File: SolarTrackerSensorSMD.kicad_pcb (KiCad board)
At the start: 2 copper layers, 94 x 70 mm, 81 parts, among them J1 Conn_01x03_Male, J10 Conn_01x01_Male, J11 Conn_01x01_Male, J12 Conn_01x01_Male, J13 Conn_01x01_Male, J14 Conn_01x01_Male, J15 Conn_01x05_Male, J16 Conn_01x05_Male, J17 Conn_01x01_Male, J18 Conn_01x01_Male, J19 Conn_01x01_Male, J2 Conn_01x03_Male, J20 Conn_01x01_Male, J21 Conn_01x01_Male, J22 Conn_01x01_Male, J23 Conn_01x01_Male, J24 Conn_01x01_Male, J3 Conn_01x03_Male, J4 Conn_01x03_Male, J5 Conn_01x07_Male, J6 Conn_01x05_Male, J7 Conn_01x01_Male, J8 Conn_01x01_Male, J9 Conn_01x01_Male, Q1 Q_Photo_NPN, Q2 Q_Photo_NPN, Q3 Q_Photo_NPN, Q4 Q_Photo_NPN, Q5 Q_Photo_NPN, Q6 Q_Photo_NPN, Q7 Q_Photo_NPN, Q8 Q_Photo_NPN, U1 LM339, U2 7404, U3 7408, U4 7408, U5 7432

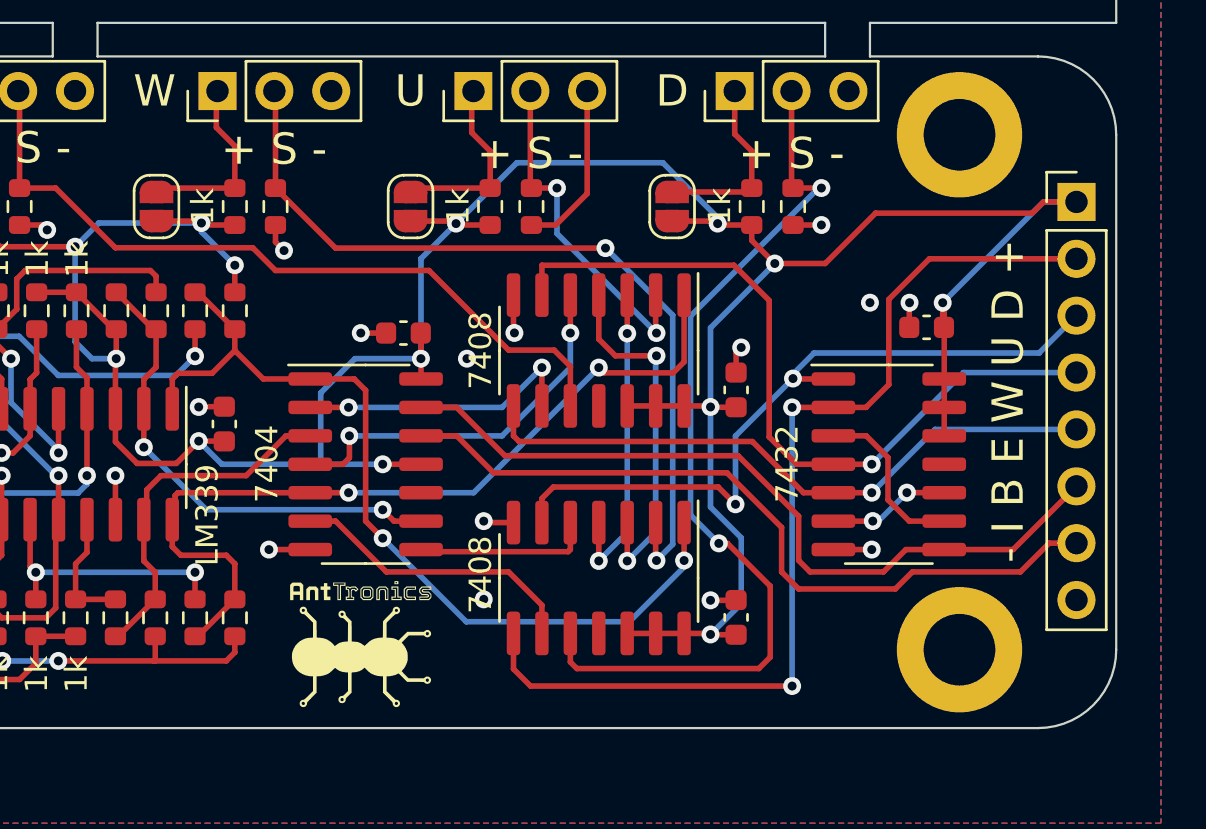
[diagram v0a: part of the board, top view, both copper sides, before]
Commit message: Replace Idle with Busy_UD & Busy_EW
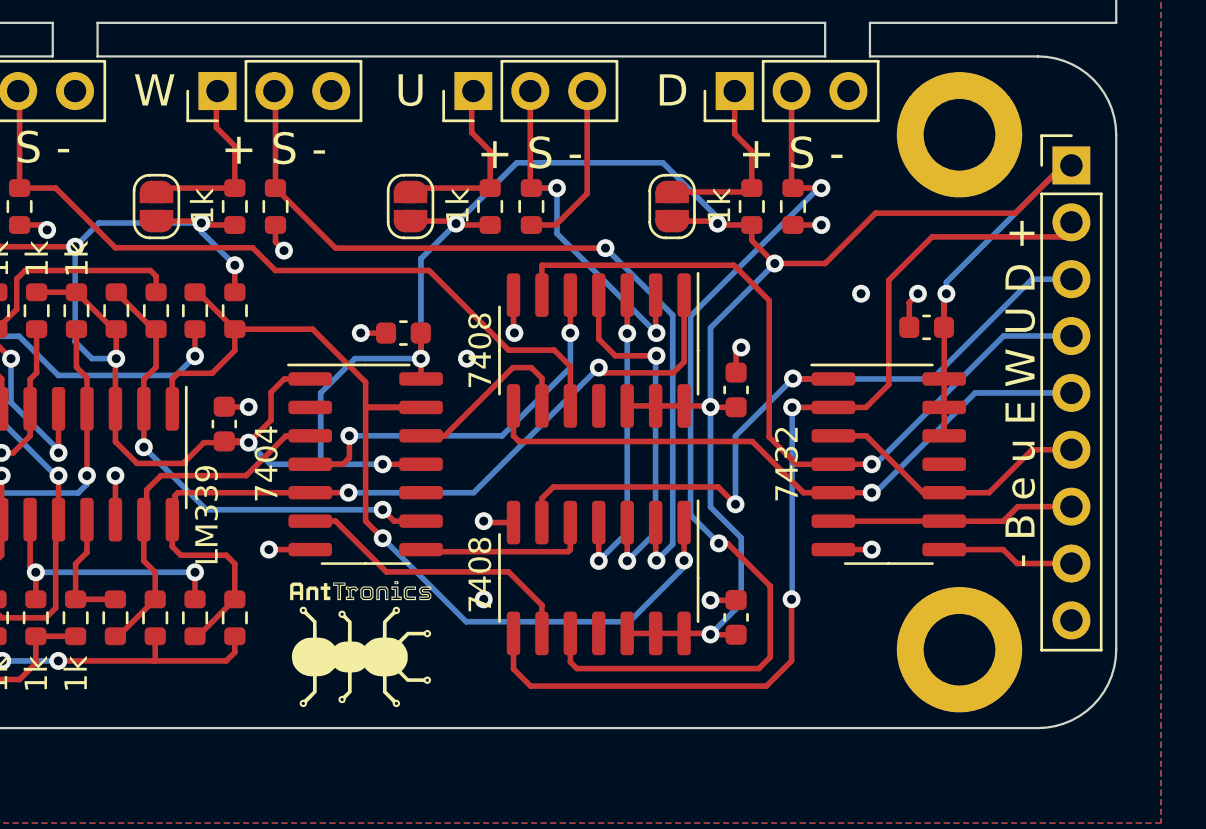
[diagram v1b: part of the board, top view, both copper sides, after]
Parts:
- J5: footprint Connector_PinHeader_2.54mm:PinHeader_1x08_P2.54mm_Vertical -> Connector_PinHeader_2.54mm:PinHeader_1x09_P2.54mm_Vertical
- moved J5 1.65 mm to (151.0, 95.9)
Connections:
- J5 pad 6: /BUSY -> /BUSY_UD
- J5 pad 7: /IDLE -> /BUSY_EW
- J5 pad 8: GND -> /BUSY
- U2 pad 1: /CW -> VCC
- U2 pad 12: /IDLE -> /NCW
- U2 pad 13: /BUSY -> /CW
- U2 pad 2: /NCW -> unconnected-(U2-Pad2)
- U5 pad 10: Net-(U5-Pad10) -> /BUSY_UD
- U5 pad 3: Net-(U5-Pad3) -> /BUSY_UD
- U5 pad 6: Net-(U5-Pad10) -> /BUSY_EW
- U5 pad 9: Net-(U5-Pad3) -> /BUSY_EW
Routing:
- net /IDLE: track 34.1 -> 0.00 mm
- net /BUSY: track 35.1 -> 6.19 mm
- net /BUSY_UD: track 0.00 -> 12.7 mm
- net /BUSY_EW: track 0.00 -> 11.2 mm
- net Net-(U5-Pad3): track 7.63 -> 0.00 mm
- net VCC: track 192.5 -> 199.8 mm
- net /CW: track 39.6 -> 45.1 mm
- net Net-(U5-Pad10): track 5.48 -> 0.00 mm, vias 2 -> 0
- net /NCW: track 12.8 -> 8.10 mm, vias 2 -> 0
- net /OW: track 34.2 -> 34.9 mm
- net /OU: track 32.7 -> 33.3 mm
- net /OD: track 44.5 -> 45.0 mm
- net GND: track 44.8 -> 45.3 mm
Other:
- board text added: "- B e u E W U D +"
- board text removed: "- I B E W U D +"

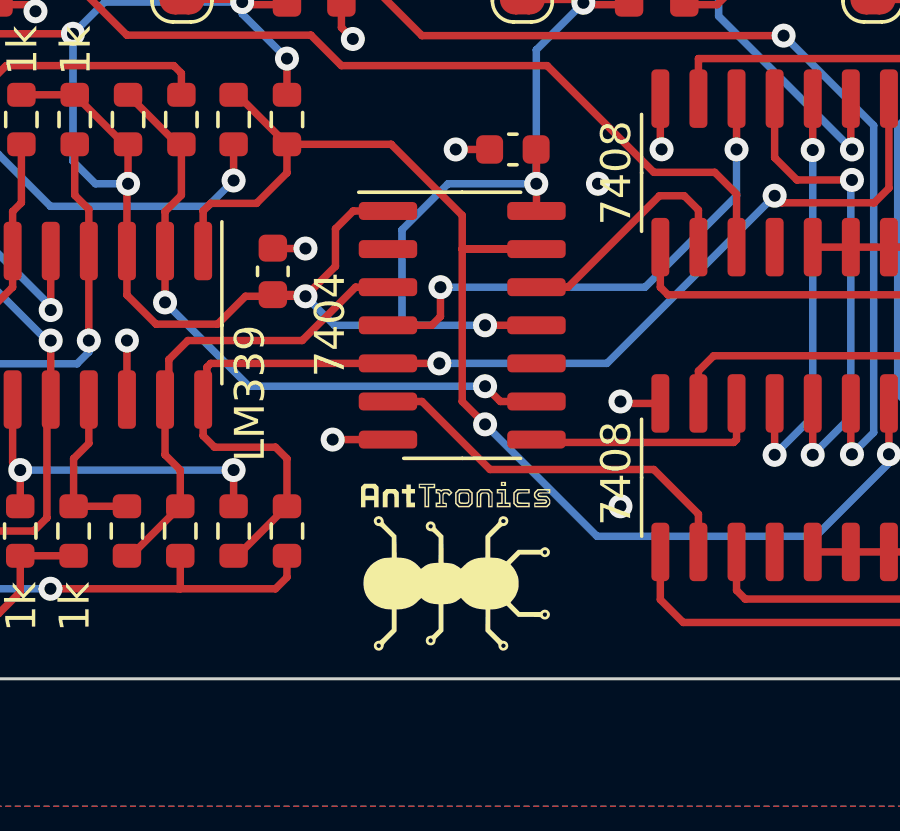
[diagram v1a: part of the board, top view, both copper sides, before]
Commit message: Add licence & reshuffle silkscreen graphics
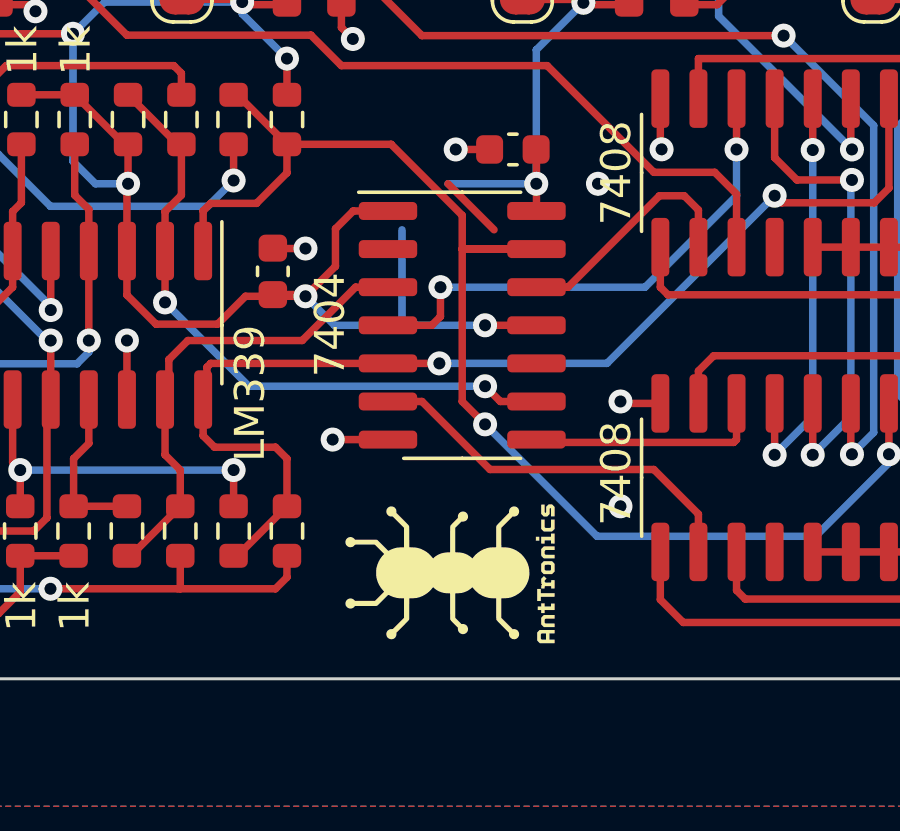
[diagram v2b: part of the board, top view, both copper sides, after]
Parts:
- removed the G*** at (119.2, 117.2)
- removed the G*** at (119.8, 102.0)
- removed the G*** at (106.5, 116.5)
- added G***: LOGO, AntTronics_Graphics:AntTronics_logo_tall_5x7, F.Cu at (119.0, 117.5)
- added G***: LOGO, LOGO, B.Cu at (125.2, 111.0)
- added G***: LOGO, AntTronics_Graphics:AntTronics_logo_square_10x10, B.Cu at (136.2, 104.5)
- added REF**: OSHW-Logo_5.7x6mm_SilkScreen, Symbol:OSHW-Logo_5.7x6mm_SilkScreen, B.Cu at (138.5, 116.0)
- moved G*** 15.7 mm to (116.2, 101.8), turned to 180 degrees
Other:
- board text added: "Copyright © 2023 Antonios Vamporakis <ant@anttronics.com> Licensed under CERN-OHL-S v2 or any later version https://github.com/anttronics/SolarTrackerSensor"
- board text added: "SPDX-FileCopyrightText: 2023 Antonios Vamporakis <ant@anttronics.com> SPDX-License-Identifier: CERN-OHL-S-2.0+ This source is distributed WITHOUT ANY EXPRESS OR IMPLIED WARRANTY, INCLUDING OF MERCHANTABILITY, SATISFACTORY QUALITY AND FITNESS FOR A PARTICULAR PURPOSE. Please see the CERN-OHL-S v2 for applicable conditions. Source location: https://github.com/anttronics/SolarTrackerSensor As per CE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"

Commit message: CERN OHL W seems more appropriate
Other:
- board text added: "Copyright © 2023 Antonios Vamporakis <ant@anttronics.com> Licensed under CERN-OHL-W v2 or any later version https://github.com/anttronics/SolarTrackerSensor"
- board text added: "SPDX-FileCopyrightText: 2023 Antonios Vamporakis <ant@anttronics.com> SPDX-License-Identifier: CERN-OHL-W-2.0+ You may redistribute and modify this documentation and make products using it under the terms of the CERN-OHL-W v2 (https:/cern.ch/cern-ohl). This documentation is distributed WITHOUT ANY EXPRESS OR IMPLIED WARRANTY, INCLUDING OF MERCHANTABILITY, SATISFACTORY QUALITY AND FITNESS FOR A PA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"
- board text removed: "Copyright © 2023 Antonios Vamporakis <ant@anttronics.com> Licensed under CERN-OHL-S v2 or any later version https://github.com/anttronics/SolarTrackerSensor"
- board text removed: "SPDX-FileCopyrightText: 2023 Antonios Vamporakis <ant@anttronics.com> SPDX-License-Identifier: CERN-OHL-S-2.0+ This source is distributed WITHOUT ANY EXPRESS OR IMPLIED WARRANTY, INCLUDING OF MERCHANTABILITY, SATISFACTORY QUALITY AND FITNESS FOR A PARTICULAR PURPOSE. Please see the CERN-OHL-S v2 for applicable conditions. Source location: https://github.com/anttronics/SolarTrackerSensor As per CE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"
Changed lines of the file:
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@@
     (effects (font (size 1.4 1.4) (thickness 0.2)) (justify mirror))
   )
-  (gr_text "Copyright © 2023 Antonios Vamporakis <ant@anttronics.com>\nLicensed under CERN-OHL-S v2 or any later version\nhttps://github.com/anttronics/SolarTrackerSensor\n" (at 134.25 115.75) (layer "B.SilkS")
+  (gr_text "Copyright © 2023 Antonios Vamporakis <ant@anttronics.com>\nLicensed under CERN-OHL-W v2 or any later version\nhttps://github.com/anttronics/SolarTrackerSensor\n" (at 134.25 115.75) (layer "B.SilkS")
     (effects (font (size 0.8 0.7) (thickness 0.15)) (justify left mirror))
   )
@@
     (effects (font (size 1.4 1.4) (thickness 0.2)))
   )
-  (gr_text "SPDX-FileCopyrightText: 2023 Antonios Vamporakis <ant@anttronics.com>\nSPDX-License-Identifier: CERN-OHL-S-2.0+\n\nThis source is distributed WITHOUT ANY EXPRESS OR IMPLIED WARRANTY, INCLUDING OF MERCHANTABILITY, SATISFACTORY QUALITY AND FITNESS FOR A \nPARTICULAR PURPOSE. Please see the CERN-OHL-S v2 for applicable conditions.\n\nSource location: https://github.com/anttronics/SolarTrackerSensor\n\nAs per CERN-OHL-S v2 section 4, should You produce hardware based on this source, You must where practicable maintain the Source Location \nvisible on the circuit board, external case or documentation of the SolarTrackerSensor or other products you make using this source.\n" (at 199 173.75) (layer "Cmts.User")
+  (gr_text "SPDX-FileCopyrightText: 2023 Antonios Vamporakis <ant@anttronics.com>\nSPDX-License-Identifier: CERN-OHL-W-2.0+\n\nYou may redistribute and modify this documentation and make products\nusing it under the terms of the CERN-OHL-W v2 (https:/cern.ch/cern-ohl).\nThis documentation is distributed WITHOUT ANY EXPRESS OR IMPLIED\nWARRANTY, INCLUDING OF MERCHANTABILITY, SATISFACTORY QUALITY\nAND FITNESS FOR A PARTICULAR PURPOSE. Please see the CERN-OHL-W v2\nfor applicable conditions.\n\nSource location: https://github.com/anttronics/SolarTrackerSensor\n\nAs per CERN-OHL-W v2 section 4.1, should You produce hardware based on\nthese sources, You must maintain the Source Location visible on the\nexternal case of the SolarTrackerSensor or other product you make using\nthis documentation.\n" (at 242.25 177.75) (layer "Cmts.User")
     (effects (font (size 0.7 0.7) (thickness 0.1)) (justify left))
   )
